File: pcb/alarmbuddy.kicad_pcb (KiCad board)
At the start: 2 copper layers, 81 x 59 mm, 24 parts, among them J1 10-16VAC, J4 3V3, J5 SENS1-3, J6 SENS4-6, J7 SENS7-9, J8 SENS10-12, J9 FTDI, U1 VXO7803-500, U3 ESP32-WROOM-32D

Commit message: v3
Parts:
- J1: value 10-16VAC -> POWER
- J9: value FTDI -> PROG
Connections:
- J9 pad 1: /~DTR -> /RTS
- J9 pad 2: /RX -> /~DTR
- J9 pad 3: /TX -> +3V3
- J9 pad 4: +3V3 -> /TX
- J9 pad 5: /RTS -> /RX
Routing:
- net /~DTR: track 39.0 -> 12.9 mm
- net /RTS: track 76.1 -> 59.4 mm
- net /RX: track 13.6 -> 23.2 mm, vias 1 -> 2
- net /TX: track 14.6 -> 17.7 mm, vias 1 -> 0
- net +3V3: track 113.1 -> 110.4 mm, vias 4 -> 2
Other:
- board text added: "alarmbuddy v3"
- board text removed: "alarmbuddy v2"

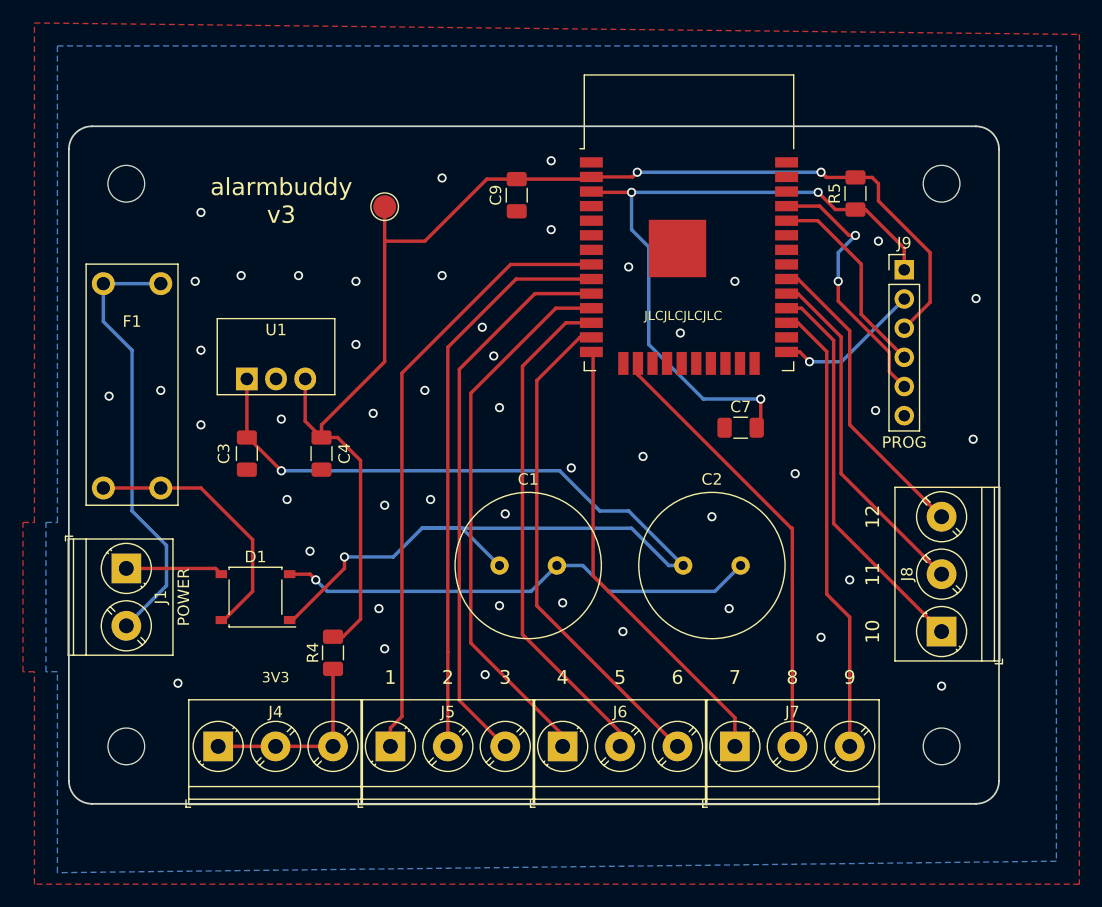
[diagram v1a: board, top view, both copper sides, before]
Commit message: esp32-s2 change
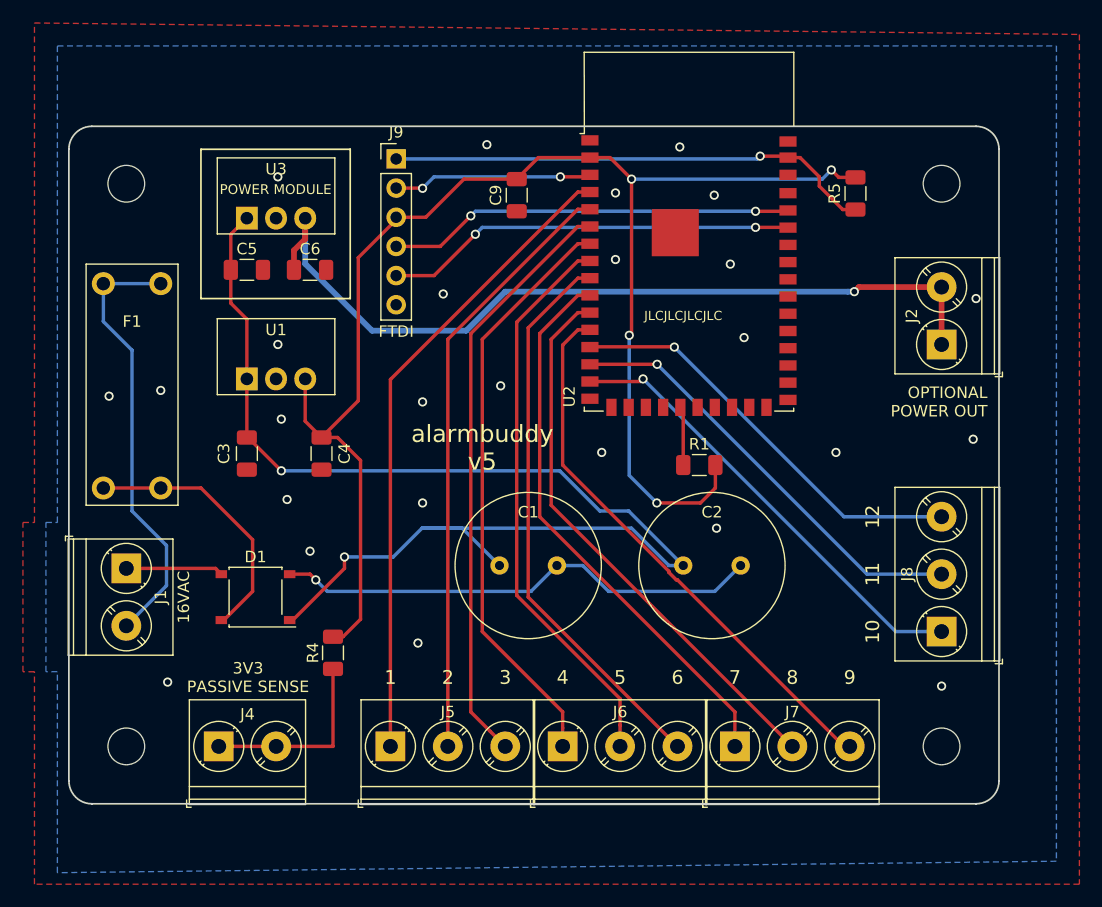
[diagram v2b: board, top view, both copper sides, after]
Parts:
- removed C7: 0.1uF, Capacitor_SMD:C_1206_3216Metric
- removed TP2: TP3V3, TestPoint:TestPoint_Pad_D2.0mm
- added C5: 10uF 50V, Capacitor_SMD:C_1206_3216Metric, F.Cu at (40.5, 42.5)
- added C6: 22uF 10V, Capacitor_SMD:C_1206_3216Metric, F.Cu at (46.0, 42.5)
- added J2: 12V, TerminalBlock_Phoenix:TerminalBlock_Phoenix_PT-1,5-2-5.0-H_1x02_P5.00mm_Horizontal, F.Cu at (101.0, 49.0)
- added R1: 10K, Resistor_SMD:R_1206_3216Metric, F.Cu at (79.9, 59.5)
- added U2: ESP32-S2-WROVER, RF_Module:ESP32-S2-WROVER, F.Cu at (79.0, 43.0)
- J1: value POWER -> 16VAC
- J4: footprint TerminalBlock_Phoenix:TerminalBlock_Phoenix_PT-1,5-3-5.0-H_1x03_P5.00mm_Horizontal -> TerminalBlock_Phoenix:TerminalBlock_Phoenix_PT-1,5-2-5.0-H_1x02_P5.00mm_Horizontal
- J9: value PROG -> FTDI
- U3: value ESP32-WROOM-32D -> VXO-78XX; footprint RF_Module:ESP32-WROOM-32 -> !Greg:VXO78-500
- moved J9 45.3 mm to (53.5, 32.8)
- moved U3 38.6 mm to (40.5, 38.0)
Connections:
- U3 pad 1: GND -> Net-(C1-Pad1)
- U3 pad 2: +3V3 -> GND
- U3 pad 3: /RTS -> +12V
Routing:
- net +12V: track 0.00 -> 73.3 mm, vias 0 -> 1
- net +3V3: track 110.4 -> 129.4 mm, vias 2 -> 4
- net /TX: track 17.7 -> 35.4 mm, vias 0 -> 2
- net /RTS: track 59.4 -> 42.5 mm, vias 3 -> 1
- net Net-(C1-Pad1): track 95.3 -> 110.5 mm
- net /RX: track 23.2 -> 35.9 mm
- net /SENSOR12: track 26.9 -> 36.8 mm, vias 0 -> 1
- net /SENSOR8: track 39.0 -> 48.5 mm
- net /SENSOR7: track 39.6 -> 48.7 mm
- net /SENSOR9: track 39.7 -> 48.6 mm
- net /SENSOR11: track 30.6 -> 38.2 mm, vias 0 -> 1
- net /SENSOR6: track 43.2 -> 49.0 mm
- net /SENSOR10: track 34.5 -> 39.8 mm, vias 0 -> 1
- net Net-(R1-Pad1): track 0.00 -> 5.13 mm
- net /SENSOR5: track 44.2 -> 49.3 mm
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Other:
- board text added: "3V3 PASSIVE SENSE"
- board text added: "OPTIONAL POWER OUT"
- board text added: "POWER MODULE"
- board text added: "alarmbuddy v5"
- board text removed: "alarmbuddy v3"

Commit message: v6 drafty
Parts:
- removed the J2 at (101.0, 49.0)
- removed U3: VXO-78XX, !Greg:VXO78-500
- added D2: SS210, Diode_SMD:D_SMA, F.Cu at (42.6, 43.6)
- added D3: SS210, Diode_SMD:D_SMA, F.Cu at (48.0, 42.8)
- added D4: SS210, Diode_SMD:D_SMA, F.Cu at (46.2, 37.3)
- added D5: SS210, Diode_SMD:D_SMA, F.Cu at (49.9, 37.3)
- added FB1: 600@100MHz, Inductor_SMD:L_0805_2012Metric, F.Cu at (45.5, 61.0)
- added L1: 4.7u, switching:L_Sunlord_MWSA0402_4.4x4.2mm, F.Cu at (50.8, 68.5)
- added R11: 100, Resistor_SMD:R_0402_1005Metric, F.Cu at (38.5, 62.9)
- added R12: 1k5, Resistor_SMD:R_0402_1005Metric, F.Cu at (38.5, 63.9)
- added R2: 470, Resistor_SMD:R_0402_1005Metric, F.Cu at (38.5, 64.9)
- C1: value 470uF 50V -> 10u; footprint Capacitor_THT:C_Radial_D12.5mm_H25.0mm_P5.00mm -> Capacitor_SMD:C_1206_3216Metric
- C2: value 470uF 50V -> 47u; footprint Capacitor_THT:C_Radial_D12.5mm_H25.0mm_P5.00mm -> Capacitor_SMD:C_1206_3216Metric
- C3: value 10uF 50V -> 47u
- C4: value 22uF 10V -> 0.1u 25v; footprint Capacitor_SMD:C_1206_3216Metric -> Capacitor_SMD:C_0603_1608Metric
- C5: value 10uF 50V -> 15nF; footprint Capacitor_SMD:C_1206_3216Metric -> Capacitor_SMD:C_0603_1608Metric
- C6: value 22uF 10V -> 470uF 50V; footprint Capacitor_SMD:C_1206_3216Metric -> Capacitor_SMD:CP_Elec_10x10
- C7: renamed from C9; value 10uF -> 10u
- D1: value 1A -> SS210; footprint Diode_SMD:Diode_Bridge_Diotec_ABS -> Diode_SMD:D_SMA
- F1: value FC-203-22 -> 140mA hold / 340mA trip mSMD014; footprint !Greg:Belfuse FC-203-22 -> Fuse:Fuse_1812_4532Metric
- J1: value 16VAC -> 24VAC; footprint TerminalBlock_Phoenix:TerminalBlock_Phoenix_PT-1,5-2-5.0-H_1x02_P5.00mm_Horizontal -> TerminalBlock_Phoenix:TerminalBlock_Phoenix_MKDS-1,5-2-5.08_1x02_P5.08mm_Horizontal
- J7: renamed from J9; value FTDI -> eflashy32
- R4: value 100R -> 100; footprint Resistor_SMD:R_1206_3216Metric -> Resistor_SMD:R_0402_1005Metric
- R5: footprint Resistor_SMD:R_1206_3216Metric -> Resistor_SMD:R_0805_2012Metric
- R6: renamed from R1; footprint Resistor_SMD:R_1206_3216Metric -> Resistor_SMD:R_0805_2012Metric
- U1: value VXO7803-500 -> BD9G101G; footprint !Greg:VXO78-500 -> Package_TO_SOT_SMD:SOT-23-6
- moved J2 69.7 mm to (101.0, 54.1), turned to 90 degrees
- moved R4 62.6 mm to (101.0, 42.5), turned to 90 degrees
- moved C2 28.1 mm to (51.3, 75.5), turned to 180 degrees
- moved C5 23.5 mm to (45.5, 65.5)
- moved J1 22.5 mm to (29.6, 46.0)
- moved C1 21.7 mm to (41.3, 72.8), turned to -90 degrees
- moved C3 18.1 mm to (51.3, 73.0), turned to 180 degrees
- moved F1 18.0 mm to (39.6, 37.0), turned to -90 degrees
- moved U1 15.6 mm to (41.8, 67.5), turned to -90 degrees
- moved J7 13.8 mm to (58.7, 45.6), turned to 180 degrees
- moved C4 11.7 mm to (38.3, 66.4), turned to 0 degrees
- moved C6 10.5 mm to (45.5, 53.0), turned to 180 degrees
- moved D1 4.33 mm to (45.5, 70.5), turned to -90 degrees
- moved R6 3.41 mm to (76.5, 59.4), turned to 180 degrees
- moved C7 2.36 mm to (65.4, 34.1)
- renumbered J4 to J2, J5 to J3, J6 to J4, J7 to J5, J8 to J6
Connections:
- C2 pad 1: Net-(C1-Pad1) -> +3V3
- C3 pad 1: Net-(C1-Pad1) -> +3V3
- C4 pad 2: GND -> /FB
- C5 pad 1: Net-(C1-Pad1) -> Net-(C5-Pad1)
- C5 pad 2: GND -> /LX
- C6 pad 1: +12V -> Net-(C6-Pad1)
- D1 pad 1: Net-(C1-Pad1) -> /LX
- F1 pad 1: Net-(D1-Pad4) -> Net-(F1-Pad1)
- F1 pad 2: Net-(F1-Pad2) -> Net-(D2-Pad1)
- J1 pad 1: Net-(D1-Pad3) -> Net-(D4-Pad1)
- J1 pad 2: Net-(F1-Pad2) -> Net-(F1-Pad1)
- J7 pad 1: /RTS -> GND
- J7 pad 2: /~DTR -> /RX
- J7 pad 3: +3V3 -> /TX
- J7 pad 4: /TX -> +3V3
- J7 pad 5: /RX -> /~{DTR}
- J7 pad 6: GND -> /RTS
- R4 pad 1: +3V3 -> /3V3_COMMON
- R4 pad 2: /3V3_COMMON -> +3V3
- U1 pad 1: Net-(C1-Pad1) -> Net-(C5-Pad1)
- U1 pad 3: +3V3 -> /FB
- U2 pad 16: (no net) -> unconnected-(U2-Pad16)
- U2 pad 17: (no net) -> unconnected-(U2-Pad17)
- U2 pad 18: (no net) -> unconnected-(U2-Pad18)
- U2 pad 19: (no net) -> unconnected-(U2-Pad19)
- U2 pad 20: (no net) -> unconnected-(U2-Pad20)
- U2 pad 22: (no net) -> unconnected-(U2-Pad22)
- U2 pad 23: (no net) -> unconnected-(U2-Pad23)
- U2 pad 24: (no net) -> unconnected-(U2-Pad24)
- U2 pad 25: (no net) -> unconnected-(U2-Pad25)
- U2 pad 27: (no net) -> unconnected-(U2-Pad27)
- U2 pad 28: (no net) -> unconnected-(U2-Pad28)
- U2 pad 29: (no net) -> unconnected-(U2-Pad29)
- U2 pad 3: /~DTR -> /~{DTR}
- U2 pad 30: (no net) -> unconnected-(U2-Pad30)
- U2 pad 31: (no net) -> unconnected-(U2-Pad31)
- U2 pad 32: (no net) -> unconnected-(U2-Pad32)
- U2 pad 33: (no net) -> unconnected-(U2-Pad33)
- U2 pad 34: (no net) -> unconnected-(U2-Pad34)
- U2 pad 35: (no net) -> unconnected-(U2-Pad35)
- U2 pad 36: (no net) -> unconnected-(U2-Pad36)
- U2 pad 39: (no net) -> unconnected-(U2-Pad39)
- U2 pad 40: (no net) -> unconnected-(U2-Pad40)
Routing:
- net +12V: track 73.3 -> 0.00 mm, vias 1 -> 0
- net Net-(C1-Pad1): track 110.5 -> 37.6 mm, vias 2 -> 0
- net GND: track 42.7 -> 87.1 mm, vias 27 -> 22
- net Net-(F1-Pad2): track 38.5 -> 0.00 mm
- net +3V3: track 129.4 -> 167.2 mm, vias 4 -> 6
- net Net-(D4-Pad1): track 0.00 -> 30.0 mm
- net Net-(C6-Pad1): track 0.00 -> 24.5 mm
- net Net-(F1-Pad1): track 0.00 -> 23.3 mm
- net Net-(D1-Pad4): track 23.1 -> 0.00 mm
- net /~{DTR}: track 0.00 -> 19.4 mm, vias 0 -> 1
- net /~DTR: track 17.4 -> 0.00 mm, vias 2 -> 0
- net Net-(D2-Pad1): track 0.00 -> 13.5 mm
- net /SENSOR10: track 39.8 -> 48.7 mm, vias 1 -> 2
- net Net-(D1-Pad3): track 8.48 -> 0.00 mm
- net /SENSOR11: track 38.2 -> 45.2 mm, vias 1 -> 2
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- added copper zone on F.Cu, net /LX
- removed copper zone on F.Cu, net GND
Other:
- net class Default removed
- net class Small removed
- board text added: "J3"
- board text added: "RTS DTR 3V3 TX RX GND"
- board text added: "alarmbuddy v6"
- board text removed: "3V3 PASSIVE SENSE"
- board text removed: "OPTIONAL POWER OUT"
- board text removed: "POWER MODULE"
- board text removed: "alarmbuddy v5"

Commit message: silkscreen
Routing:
- net +3V3: track 167.2 -> 166.3 mm
- net /RTS: track 38.0 -> 37.1 mm
- net Net-(C6-Pad1): track 24.5 -> 24.0 mm
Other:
- board text added: "24VAC"
- board text added: "3.3V"
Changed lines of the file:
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@@
     (property "Sheetname" "")
     (attr smd)
-    (fp_text reference "R5" (at 0 -1.65 90) (layer "F.SilkS")
+    (fp_text reference "R5" (at 0 -1.65 90) (layer "F.SilkS") hide
       (effects (font (size 1 1) (thickness 0.15)))
     )
@@
     (property "Sheetname" "")
     (attr smd)
-    (fp_text reference "R4" (at 0 -1.17 90) (layer "F.SilkS")
+    (fp_text reference "R4" (at 0 -1.17 90) (layer "F.SilkS") hide
       (effects (font (size 1 1) (thickness 0.15)))
     )
@@
     (property "Sheetname" "")
     (attr smd)
-    (fp_text reference "R6" (at 0 -1.65 180) (layer "F.SilkS")
+    (fp_text reference "R6" (at 0 -1.65 180) (layer "F.SilkS") hide
       (effects (font (size 1 1) (thickness 0.15)))
     )
@@
   (gr_text "RTS\n\nDTR\n\n3V3\n\nTX\n\nRX\n\nGND" (at 55.2 37.6) (layer "F.SilkS")
     (effects (font (size 0.635 0.7) (thickness 0.1)))
+  )
+  (gr_text "3.3V" (at 101.2 45) (layer "F.SilkS")
+    (effects (font (size 1.5 1.5) (thickness 0.3)))
+  )
+  (gr_text "24VAC" (at 30.2 56) (layer "F.SilkS")
+    (effects (font (size 1.5 1.5) (thickness 0.3)))
   )
   (gr_text "J3" (at -18.9 39.16) (layer "F.Fab")
@@
   (segment (start 37.55 66.4) (end 36.2 66.4) (width 0.4) (layer "F.Cu") (net 2))
   (segment (start 52.8 68.65) (end 52.8 72.475) (width 1) (layer "F.Cu") (net 2))
-  (segment (start 101.2 41) (end 101 41.2) (width 0.5) (layer "F.Cu") (net 2))
   (segment (start 53.625 77.975) (end 55.8 75.8) (width 1) (layer "F.Cu") (net 2))
   (segment (start 51.05 78.5) (end 36.05 78.5) (width 0.3) (layer "F.Cu") (net 2))
   (segment (start 65.4 32.7) (end 70.35 32.7) (width 0.5) (layer "F.Cu") (net 2))
-  (segment (start 99.1 39.6) (end 101.2 39.6) (width 0.5) (layer "F.Cu") (net 2))
   (segment (start 58.7 37.98) (end 59.35 37.98) (width 1) (layer "F.Cu") (net 2))
   (segment (start 36.05 67.5) (end 37.55 67.5) (width 0.3) (layer "F.Cu") (net 2))
   (segment (start 56 59.6) (end 55.8 59.4) (width 0.3) (layer "F.Cu") (net 2))
-  (segment (start 93.95 34.45) (end 99.1 39.6) (width 0.5) (layer "F.Cu") (net 2))
   (segment (start 63 32.9) (end 63.2 32.7) (width 1) (layer "F.Cu") (net 2))
   (segment (start 51.3 78.25) (end 51.05 78.5) (width 0.3) (layer "F.Cu") (net 2))
   (segment (start 75.4 59.5) (end 73.5 59.5) (width 0.3) (layer "F.Cu") (net 2))
-  (segment (start 93.6 32.7) (end 93.6 34.35) (width 0.5) (layer "F.Cu") (net 2))
   (segment (start 38.95 60.9) (end 39.06 61.01) (width 0.4) (layer "F.Cu") (net 2))
-  (segment (start 101 41.2) (end 101 41.98) (width 0.5) (layer "F.Cu") (net 2))
   (segment (start 39.06 61.01) (end 39.06 62.9) (width 0.4) (layer "F.Cu") (net 2))
   (segment (start 52.8 72.475) (end 52.65 72.625) (width 1) (layer "F.Cu") (net 2))
-  (segment (start 101.2 39.6) (end 101.2 41) (width 0.5) (layer "F.Cu") (net 2))
   (segment (start 52.775 73) (end 52.775 75.5) (width 1) (layer "F.Cu") (net 2))
+  (segment (start 93.5 34.9375) (end 94.7375 34.9375) (width 0.5) (layer "F.Cu") (net 2))
   (segment (start 70.5 32.6) (end 70.375 32.725) (width 0.5) (layer "F.Cu") (net 2))
   (segment (start 52.775 77.975) (end 51.575 77.975) (width 0.3) (layer "F.Cu") (net 2))
   (segment (start 73.5 59.5) (end 73.4 59.6) (width 0.3) (layer "F.Cu") (net 2))
+  (segment (start 101 41.2) (end 101 41.98) (width 0.5) (layer "F.Cu") (net 2))
   (segment (start 59.35 37.98) (end 63 34.33) (width 1) (layer "F.Cu") (net 2))
   (segment (start 63 34.33) (end 63 32.9) (width 1) (layer "F.Cu") (net 2))
   (segment (start 55.8 75.8) (end 55.8 59.4) (width 1) (layer "F.Cu") (net 2))
   (segment (start 35.6 62.45) (end 37.15 60.9) (width 0.4) (layer "F.Cu") (net 2))
+  (segment (start 93.6 32.7) (end 93.6 34.8375) (width 0.5) (layer "F.Cu") (net 2))
   (segment (start 84.1505 32.6) (end 70.5 32.6) (width 0.5) (layer "F.Cu") (net 2))
   (segment (start 52.775 77.975) (end 53.625 77.975) (width 1) (layer "F.Cu") (net 2))
   (segment (start 37.55 67.5) (end 37.55 66.4) (width 0.3) (layer "F.Cu") (net 2))
   (segment (start 35.6 65.8) (end 35.6 62.45) (width 0.4) (layer "F.Cu") (net 2))
+  (segment (start 94.7375 34.9375) (end 101 41.2) (width 0.5) (layer "F.Cu") (net 2))
+  (segment (start 93.6 34.8375) (end 93.5 34.9375) (width 0.5) (layer "F.Cu") (net 2))
   (segment (start 63.2 32.7) (end 65.4 32.7) (width 1) (layer "F.Cu") (net 2))
   (segment (start 57.02 37.98) (end 58.7 37.98) (width 1) (layer "F.Cu") (net 2))
-  (segment (start 93.5 34.45) (end 93.95 34.45) (width 0.5) (layer "F.Cu") (net 2))
-  (segment (start 93.6 34.35) (end 93.5 34.45) (width 0.5) (layer "F.Cu") (net 2))
   (segment (start 52.65 68.5) (end 52.8 68.65) (width 1) (layer "F.Cu") (net 2))
   (segment (start 55.8 59.4) (end 55.8 39.2) (width 1) (layer "F.Cu") (net 2))
@@
   (segment (start 59.74 34.4) (end 58.7 35.44) (width 0.5) (layer "B.Cu") (net 5))
   (segment (start 75.7 33.5495) (end 75.8495 33.4) (width 0.5) (layer "F.Cu") (net 6))
-  (segment (start 90.8 34.65) (end 90.8 35.8) (width 0.5) (layer "F.Cu") (net 6))
   (segment (start 86.2375 32.725) (end 87.625 32.725) (width 0.5) (layer "F.Cu") (net 6))
-  (segment (start 90.8 35.8) (end 92.25 37.25) (width 0.5) (layer "F.Cu") (net 6))
+  (segment (start 88.875 32.725) (end 92.9125 36.7625) (width 0.5) (layer "F.Cu") (net 6))
+  (segment (start 92.9125 36.7625) (end 93.5 36.7625) (width 0.5) (layer "F.Cu") (net 6))
   (segment (start 75.8495 33.4) (end 85.5625 33.4) (width 0.5) (layer "F.Cu") (net 6))
-  (segment (start 88.875 32.725) (end 90.8 34.65) (width 0.5) (layer "F.Cu") (net 6))
-  (segment (start 92.25 37.25) (end 93.5 37.25) (width 0.5) (layer "F.Cu") (net 6))
+  (segment (start 87.625 32.725) (end 88.875 32.725) (width 0.5) (layer "F.Cu") (net 6))
   (segment (start 85.5625 33.4) (end 86.2375 32.725) (width 0.5) (layer "F.Cu") (net 6))
-  (segment (start 87.625 32.725) (end 88.875 32.725) (width 0.5) (layer "F.Cu") (net 6))
   (via (at 75.7 33.5495) (size 0.8) (drill 0.5) (layers "F.Cu" "B.Cu") (net 6))
   (segment (start 75.6505 33.5) (end 72.9 33.5) (width 0.5) (layer "B.Cu") (net 6))
@@
   (segment (start 43.8125 66.3625) (end 44.675 65.5) (width 0.6) (layer "F.Cu") (net 45))
   (segment (start 42.75 66.3625) (end 43.8125 66.3625) (width 0.6) (layer "F.Cu") (net 45))
-  (segment (start 49.15 41.9) (end 50.05 42.8) (width 1) (layer "F.Cu") (net 46))
   (segment (start 47.45 53) (end 45.45 55) (width 1) (layer "F.Cu") (net 46))
-  (segment (start 49.15 40) (end 49.15 41.9) (width 1) (layer "F.Cu") (net 46))
   (segment (start 50.05 42.8) (end 49.25 43.6) (width 1) (layer "F.Cu") (net 46))
+  (segment (start 49.85 39.3) (end 49.85 42.6) (width 1) (layer "F.Cu") (net 46))
   (segment (start 49.25 52.8) (end 49.45 53) (width 1) (layer "F.Cu") (net 46))
   (segment (start 49.25 43.6) (end 49.25 52.8) (width 1) (layer "F.Cu") (net 46))
   (segment (start 45.45 55) (end 45.45 59.9375) (width 1) (layer "F.Cu") (net 46))
-  (segment (start 49.85 39.3) (end 49.15 40) (width 1) (layer "F.Cu") (net 46))
+  (segment (start 49.85 42.6) (end 50.05 42.8) (width 1) (layer "F.Cu") (net 46))
   (segment (start 49.45 53) (end 47.45 53) (width 1) (layer "F.Cu") (net 46))
   (segment (start 39.05 43.2) (end 39.05 39.713541) (width 1) (layer "F.Cu") (net 47))
